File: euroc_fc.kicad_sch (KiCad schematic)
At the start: 143 parts, among them J1 Micro-Fit, J10 USB_C_Receptacle_USB2.0, J11 SWD Header, J2 Micro-Fit, J3 Micro-Fit, J4 SMA, J5 JST-GH, J6 JST-GH, J7 JST-GH, J8 JST-GH, J9 Micro_SD_Card_Det, Q1 DMN2056U, Q2 AOSP21321, Q3 DMN2056U, Q4 AOSP21321, Q5 DMN2056U, Q6 DMN2056U, Q7 DMN2056U, SW1 EVQ-PUC02K, SW2 EVQ-PUC02K, U1 STM32F401RCT6, U10 Ai-Thinker-Ra-01, U11 W25Q256JVF, U2 L7805, U3 L7805, U4 AZ1117I-3.3, U5 LSM6DSR, U6 ADXL375, U7 MS5611-01BA, U8 BMM150, U9 SAM-M8Q, Y1 25M, 18p

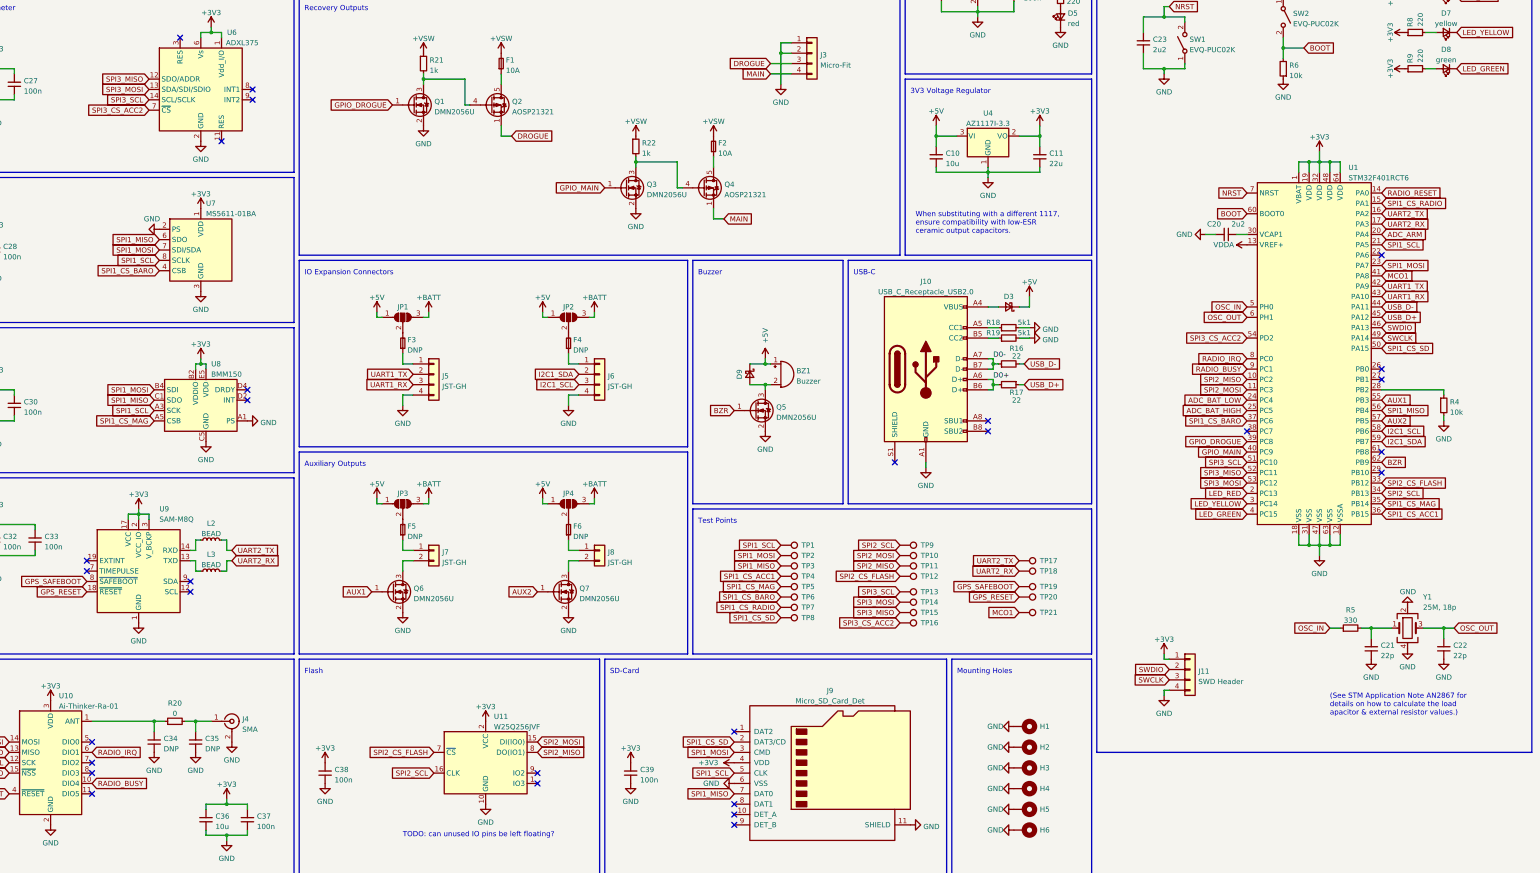
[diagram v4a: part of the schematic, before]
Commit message: Add CAN bus controller, transceiver & connectors
- Accelerometer 2 is removed from SPI for now, to be replaced
- Flash moved from SPI2 to SPI3
- SPI2 is used for CAN bus (also SD Card)
- ADC voltage dividers moved to right of PCB, IO connectors removed to
  make room
- Minor pinout changes.
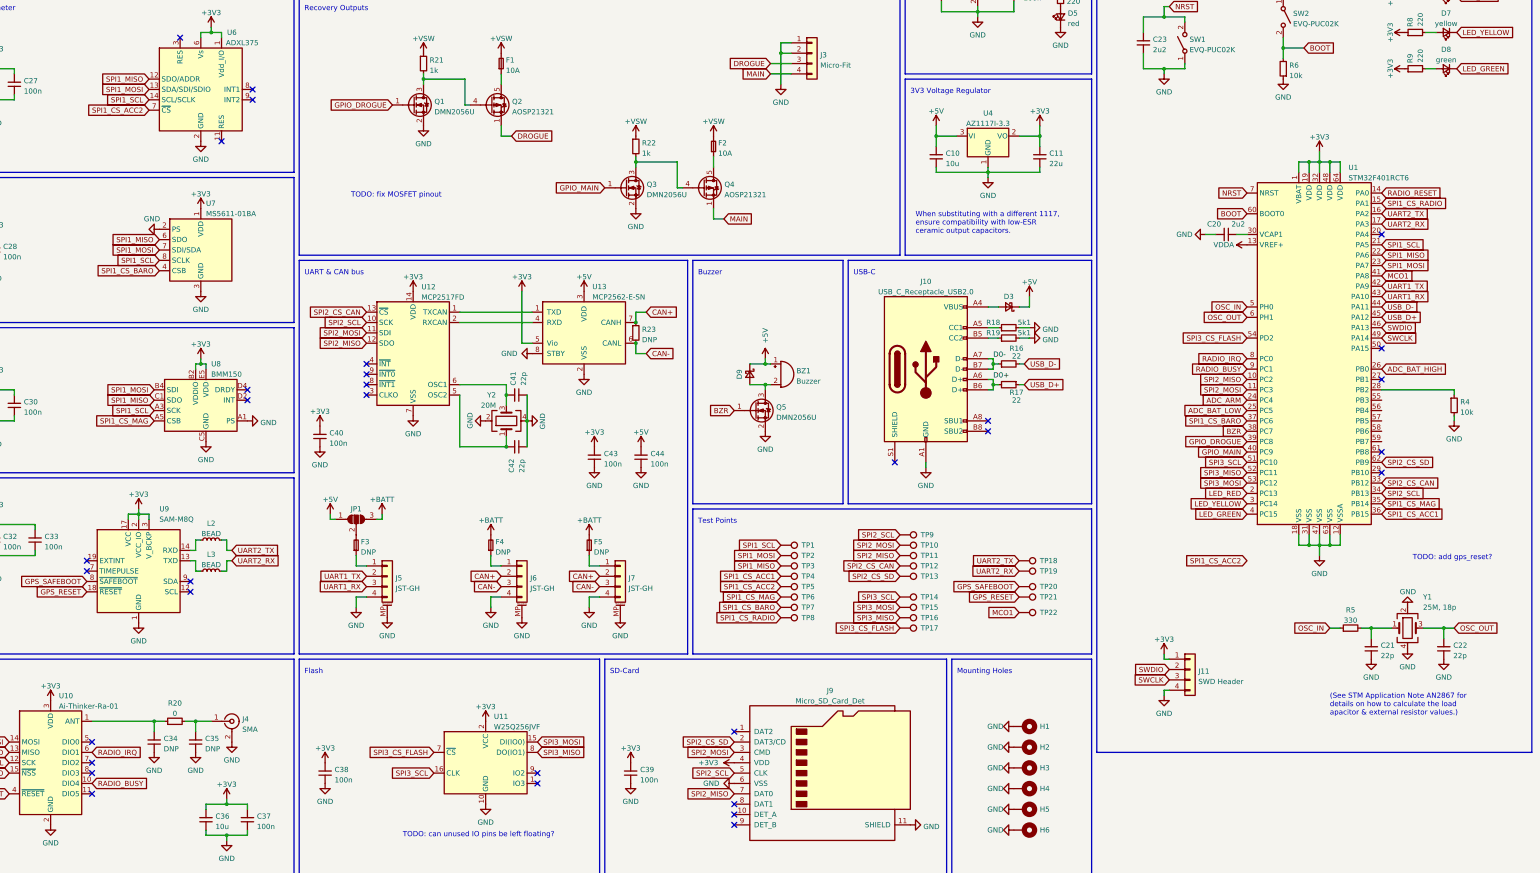
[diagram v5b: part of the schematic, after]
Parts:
- removed F6: DNP, Fuse:Fuse_1206_3216Metric, symbol Device:Fuse_Small
- removed J7, J8: JST-GH, Connector_JST:JST_GH_SM02B-GHS-TB_1x02-1MP_P1.25mm_Horizontal, symbol Connector_Generic:Conn_01x02
- removed JP2, JP3, JP4: SolderJumper_3_Open, Jumper:SolderJumper-3_P1.3mm_Open_RoundedPad1.0x1.5mm_NumberLabels, symbol Jumper:SolderJumper_3_Open
- removed Q6, Q7: DMN2056U, Package_TO_SOT_SMD:SOT-23, symbol Transistor_FET:DMG2302U
- added C40, C43, C44: 100n, Capacitor_SMD:C_0603_1608Metric, symbol Device:C_Small
- added C41, C42: 22p, Capacitor_SMD:C_0603_1608Metric, symbol Device:C_Small
- added J7: JST-GH, Connector_JST:JST_GH_SM04B-GHS-TB_1x04-1MP_P1.25mm_Horizontal, symbol Connector_Generic_MountingPin:Conn_01x04_MountingPin
- added R23: DNP, Resistor_SMD:R_0603_1608Metric, symbol Device:R_Small
- added TP22: TestPoint, TestPoint:TestPoint_Pad_D1.0mm, symbol Connector:TestPoint
- added U12: MCP2517FD, Package_SO:SOIC-14_3.9x8.7mm_P1.27mm, symbol euroc_fc:MCP2517FD
- added U13: MCP2562-E-SN, Package_SO:SOIC-8_3.9x4.9mm_P1.27mm, symbol Interface_CAN_LIN:MCP2562-E-SN
- added Y2: 20M, Oscillator:Oscillator_SMD_SeikoEpson_SG210-4Pin_2.5x2.0mm, symbol Device:Crystal_GND24
- J5, J6: symbol Connector_Generic:Conn_01x04 -> Connector_Generic_MountingPin:Conn_01x04_MountingPin
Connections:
- net +3V3: now also C40.2, C43.2, U12.14 (VDD), U13.5 (Vio)
- net +5V: now also C44.2, U13.3 (VDD)
- net +BATT: now also F4.2, F5.2
- net ADC_ARM: now also U1.24 (PC4); no longer U1.20 (PA4)
- net ADC_BAT_HIGH: now also U1.26 (PB0); no longer U1.25 (PC5)
- net ADC_BAT_LOW: now also U1.25 (PC5); no longer U1.24 (PC4)
- net BZR: now also U1.38 (PC7); no longer U1.62 (PB9)
- net GND: now also J5.MP (MountPin), J6.MP (MountPin), C40.1, C41.1, C42.1, C43.1, C44.1, J7.4 (Pin_4), J7.MP (MountPin), U12.7 (VSS), U13.2 (VSS), U13.8 (STBY), Y2.2, Y2.4
- net GPS_RESET: now also TP21.1; no longer TP20.1
- net GPS_SAFEBOOT: now also TP20.1; no longer TP19.1
- net MCO1: now also TP22.1; no longer TP21.1
- net SPI1_CS_BARO: now also TP7.1; no longer TP6.1
- net SPI1_CS_MAG: now also TP6.1; no longer TP5.1
- net SPI1_CS_RADIO: now also TP8.1; no longer TP7.1
- net SPI1_MISO: now also U1.22 (PA6), U6.12 (SDO/ADDR); no longer J9.7 (DAT0), U1.56 (PB4)
- net SPI1_MOSI: now also U6.13 (SDA/SDI/SDIO); no longer J9.3 (CMD)
- net SPI1_SCL: now also U6.14 (SCL/SCLK); no longer J9.5 (CLK)
- net SPI2_MISO: now also J9.7 (DAT0), U12.12 (SDO); no longer U11.8 (DO(IO1))
- net SPI2_MOSI: now also J9.3 (CMD), U12.11 (SDI); no longer U11.15 (DI(IO0))
- net SPI2_SCL: now also J9.5 (CLK), U12.10 (SCK); no longer U11.16 (CLK)
- net SPI3_MISO: now also TP16.1, U11.8 (DO(IO1)); no longer TP15.1, U6.12 (SDO/ADDR)
- net SPI3_MOSI: now also TP15.1, U11.15 (DI(IO0)); no longer TP14.1, U6.13 (SDA/SDI/SDIO)
- net SPI3_SCL: now also TP14.1, U11.16 (CLK); no longer TP13.1, U6.14 (SCL/SCLK)
- net UART2_RX: now also TP19.1; no longer TP18.1
- net UART2_TX: now also TP18.1; no longer TP17.1
- net at F5.1: now also J7.1 (Pin_1)
- net AUX1: no longer names the net of U1.55 (PB3)
- net AUX2: no longer names the net of U1.57 (PB5)
- net I2C1_SCL: no longer names the net of U1.58 (PB6)
- net I2C1_SCL: no longer J6.3 (Pin_3)
- net I2C1_SDA: no longer names the net of U1.59 (PB7)
- net I2C1_SDA: no longer J6.2 (Pin_2)
- removed net SPI1_CS_SD: J9.2 (DAT3/CD), TP8.1, U1.50 (PA15)
- net SPI2_CS_FLASH renamed SPI2_CS_CAN
- net SPI2_CS_CAN: now also U12.13 (~{CS}); no longer U11.7 (~{CS})
- removed net SPI3_CS_ACC2: TP16.1, U1.54 (PD2), U6.7 (~{CS})
- new net: U12.1 (TXCAN), U13.1 (TXD)
- new net: U12.2 (RXCAN), U13.4 (RXD)
- new net: C42.2, U12.5 (OSC2), Y2.1
- new net: C41.2, U12.6 (OSC1), Y2.3
- new net CAN+: J6.2 (Pin_2), J7.2 (Pin_2), R23.1, U13.7 (CANH)
- new net CAN-: J6.3 (Pin_3), J7.3 (Pin_3), R23.2, U13.6 (CANL)
- new net SPI1_CS_ACC2: TP5.1, U6.7 (~{CS})
- new net SPI2_CS_SD: J9.2 (DAT3/CD), TP13.1, U1.62 (PB9)
- new net SPI3_CS_FLASH: TP17.1, U1.54 (PD2), U11.7 (~{CS})
- no-connect marks 31 -> 34
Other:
- note added: "TODO: add gps_reset?"
- note added: "TODO: fix MOSFET pinout"
- note added: "UART & CAN bus"
- note removed: "Auxiliary Outputs"
- note removed: "IO Expansion Connectors"
- moved on the sheet: F3, F4, F5, JP1, R4, TP10, TP11, TP12, TP13, TP14, TP15, TP16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

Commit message: Replace backup acc., magnetometer
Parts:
- removed U8: BMM150, Package_CSP:WLCSP-12_1.56x1.56mm_P0.4mm, symbol Sensor_Magnetic:BMM150
- added C45: 1u, Capacitor_SMD:C_0805_2012Metric, symbol Device:C_Small
- added U8: LIS3MDL, Package_LGA:LGA-12_2x2mm_P0.5mm, symbol Sensor_Magnetic:LIS3MDL
- C20: value 2u2 -> 4u7; footprint Capacitor_SMD:C_0805_2012Metric -> Capacitor_SMD:C_1206_3216Metric; LCSC# C377773 -> C1872; Part# CL21A225KBQNNNE -> CL31B475KAHNNNE
- C23: value 2u2 -> 100n; footprint Capacitor_SMD:C_0805_2012Metric -> Capacitor_SMD:C_0603_1608Metric; LCSC# C377773 -> C1591; Part# CL21A225KBQNNNE -> CL10B104KB8NNNC
- C26: value 1u -> 10u; footprint Capacitor_SMD:C_0805_2012Metric -> Capacitor_SMD:C_1206_3216Metric; LCSC# C318694 -> C14860; Part# CL21A105KBCLNNC -> CL31B106KAHNNNE
- TP1, TP10, TP11, TP12, TP13, TP14, TP15, TP16, TP17, TP18, TP19, TP2, TP20, TP21, TP22, TP3, TP4, TP5, TP6, TP7, TP8, TP9: footprint TestPoint:TestPoint_Pad_D1.0mm -> TestPoint:TestPoint_Pad_D2.0mm
- U6: value ADXL375 -> H3LIS331DL; footprint Package_LGA:LGA-14_3x5mm_P0.8mm_LayoutBorder1x6y -> Package_LGA:LGA-16_3x3mm_P0.5mm_LayoutBorder3x5y; symbol Sensor_Motion:ADXL343 -> euroc_fc:H3LIS331DL; DigiKey# 505-ADXL375BCCZ-ND -> (none); Manufacturer Analog Devices Inc. -> (none); Part# ADXL375BCCZ -> (none)
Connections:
- net +3V3: now also U6.14 (VDD), U6.15 (reserved), C45.2, U8.5 (Vdd), U8.6 (Vdd_IO); no longer C30.2, U6.6 (Vs)
- net GND: now also U6.10 (reserved), U6.12 (GND), U6.13 (GND), U6.16 (GND), C45.1, U8.12 (GND), U8.2 (GND), U8.3 (GND); no longer U6.2 (GND), U6.4 (GND)
- net SPI1_CS_ACC2: now also U1.20 (PA4), U6.8 (~{CS}); no longer U6.7 (~{CS})
- net SPI1_CS_MAG: now also U1.29 (PB10), U8.10 (~{CS}); no longer U1.35 (PB14)
- net SPI1_MISO: now also U6.7 (SDO), U8.9 (SDO/SA1); no longer U6.12 (SDO/ADDR)
- net SPI1_MOSI: now also U6.6 (SDI), U8.11 (SDA/SDI/SDO); no longer U6.13 (SDA/SDI/SDIO)
- net SPI1_SCL: now also U6.4 (SCK), U8.1 (SCL/SPC); no longer U6.14 (SCL/SCLK)
- new net: C30.2, U8.4 (C1)
- no-connect marks 34 -> 36
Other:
- moved on the sheet: C27, C28, C29, C30, U7

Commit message: Finish rev. 2
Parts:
- C41, C42: value 22p -> 10p; LCSC# C1653 -> (none); Manufacturer Samsung Electro-Mechanics -> (none); Part# CL10C220JB8NNNC -> (none)
- Y2: footprint Oscillator:Oscillator_SMD_SeikoEpson_SG210-4Pin_2.5x2.0mm -> Crystal:Crystal_SMD_2016-4Pin_2.0x1.6mm; LCSC# C255956 -> C255878; Part# Q24FA20H0039000 -> Q22FA12800335
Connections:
- net DROGUE: now also Q2.5 (D), Q2.6 (D), Q2.7 (D), Q2.8 (D); no longer Q2.1 (S), Q2.2 (S), Q2.3 (S)
- net GPS_RESET: now also U1.61 (PB8)
- net MAIN: now also Q4.5 (D), Q4.6 (D), Q4.7 (D), Q4.8 (D); no longer Q4.1 (S), Q4.2 (S), Q4.3 (S)
- new net: F2.1, Q4.1 (S), Q4.2 (S), Q4.3 (S)
- new net: F1.1, Q2.1 (S), Q2.2 (S), Q2.3 (S)
- no-connect marks 36 -> 35
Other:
- note removed: "TODO: add gps_reset?"
- note removed: "TODO: can unused IO pins be left floating?"
- note removed: "TODO: fix MOSFET pinout"
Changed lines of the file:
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@@
   (no_connect (at 369.57 160.02))
   (no_connect (at 369.57 190.5))
-  (no_connect (at 369.57 177.8))
   (no_connect (at 369.57 170.18))
   (no_connect (at 369.57 172.72))
@@
     (effects (font (size 1.27 1.27)) (justify left bottom))
   )
-  (text "TODO: can unused IO pins be left floating?" (at 129.54 272.415 0)
-    (effects (font (size 1.27 1.27)) (justify left bottom))
-  )
   (text "USB-C" (at 240.03 134.62 0)
     (effects (font (size 1.27 1.27)) (justify left bottom))
@@
     (effects (font (size 1.27 1.27)) (justify left bottom))
   )
-  (text "TODO: add gps_reset?" (at 377.19 204.47 0)
-    (effects (font (size 1.27 1.27)) (justify left bottom))
-  )
   (text "Buzzer" (at 201.93 134.62 0)
     (effects (font (size 1.27 1.27)) (justify left bottom))
@@
     (effects (font (size 1.27 1.27)) (justify left bottom))
   )
-  (text "TODO: fix MOSFET pinout" (at 116.84 115.57 0)
-    (effects (font (size 1.27 1.27)) (justify left bottom))
-  )
   (label "D0-" (at 274.32 154.94 0)
     (effects (font (size 1.27 1.27)) (justify left bottom))
@@
     )
   )
+  (global_label "GPS_RESET" (shape input) (at 369.57 177.8 0) (fields_autoplaced)
+    (effects (font (size 1.27 1.27)) (justify left))
+    (property "Intersheet References" "${INTERSHEET_REFS}" (id 0) (at 382.4455 177.8794 0)
+      (effects (font (size 1.27 1.27)) (justify left) hide)
+    )
+  )
   (global_label "RADIO_IRQ" (shape input) (at 336.55 154.94 180) (fields_autoplaced)
     (effects (font (size 1.27 1.27)) (justify right))
@@
       (effects (font (size 1.27 1.27)) (justify right))
     )
-    (property "Value" "22p" (id 1) (at 158.75 182.88 0)
+    (property "Value" "10p" (id 1) (at 158.75 182.88 0)
       (effects (font (size 1.27 1.27)) (justify right))
     )
@@
       (effects (font (size 1.27 1.27)) hide)
     )
-    (property "LCSC#" "C1653" (id 5) (at 157.48 176.53 0)
+    (property "LCSC#" "" (id 5) (at 157.48 176.53 0)
       (effects (font (size 1.27 1.27)) hide)
     )
-    (property "Manufacturer" "Samsung Electro-Mechanics" (id 6) (at 157.48 176.53 0)
+    (property "Manufacturer" "" (id 6) (at 157.48 176.53 0)
       (effects (font (size 1.27 1.27)) hide)
     )
-    (property "Part#" "CL10C220JB8NNNC" (id 7) (at 157.48 176.53 0)
+    (property "Part#" "" (id 7) (at 157.48 176.53 0)
       (effects (font (size 1.27 1.27)) hide)
     )
@@
       (effects (font (size 1.27 1.27)) hide)
     )
-    (property "Datasheet" "https://ww1.microchip.com/downloads/en/DeviceDoc/MCP2515-Stand-Alone-CAN-Controller-with-SPI-20001801J.pdf" (id 3) (at 80.01 115.57 0)
+    (property "Datasheet" "https://www.st.com/content/ccc/resource/technical/document/datasheet/3e/48/02/c7/a4/e6/41/bb/DM00053090.pdf/files/DM00053090.pdf/jcr:content/translations/en.DM00053090.pdf" (id 3) (at 80.01 115.57 0)
       (effects (font (size 1.27 1.27)) hide)
     )
@@
   )
   (symbol (lib_id "Sensor_Magnetic:LIS3MDL") (at 76.2 161.29 0) (unit 1)
-    (in_bom yes) (on_board yes) (fields_autoplaced)
-    (property "Reference" "U8" (id 0) (at 78.2194 173.4804 0)
+    (in_bom yes) (on_board yes)
+    (property "Reference" "U8" (id 0) (at 80.01 147.32 0)
       (effects (font (size 1.27 1.27)) (justify left))
     )
-    (property "Value" "LIS3MDL" (id 1) (at 78.2194 176.0173 0)
+    (property "Value" "LIS3MDL" (id 1) (at 80.01 149.86 0)
       (effects (font (size 1.27 1.27)) (justify left))
     )
@@
       (effects (font (size 1.27 1.27)) (justify left))
     )
-    (property "Footprint" "Oscillator:Oscillator_SMD_SeikoEpson_SG210-4Pin_2.5x2.0mm" (id 2) (at 154.94 170.18 0)
+    (property "Footprint" "Crystal:Crystal_SMD_2016-4Pin_2.0x1.6mm" (id 2) (at 154.94 170.18 0)
       (effects (font (size 1.27 1.27)) hide)
     )
@@
       (effects (font (size 1.27 1.27)) hide)
     )
-    (property "Part#" "Q24FA20H0039000" (id 7) (at 154.94 170.18 0)
+    (property "Part#" "Q22FA12800335" (id 7) (at 154.94 170.18 0)
       (effects (font (size 1.27 1.27)) hide)
     )
@@
       (effects (font (size 1.27 1.27)) hide)
     )
-    (property "LCSC#" "C255956" (id 8) (at 154.94 170.18 0)
+    (property "LCSC#" "C255878" (id 8) (at 154.94 170.18 0)
       (effects (font (size 1.27 1.27)) hide)
     )
@@
     (pin "2")
   )
-  (symbol (lib_id "euroc_fc:AOSP21321") (at 151.13 92.71 0) (unit 1)
+  (symbol (lib_id "euroc_fc:AOSP21321") (at 151.13 92.71 0) (mirror x) (unit 1)
     (in_bom yes) (on_board yes) (fields_autoplaced)
     (property "Reference" "Q2" (id 0) (at 156.337 91.8753 0)
@@
       (effects (font (size 1.27 1.27)) (justify left))
     )
-    (property "Footprint" "Package_SO:SO-8_3.9x4.9mm_P1.27mm" (id 2) (at 156.21 94.615 0)
+    (property "Footprint" "Package_SO:SO-8_3.9x4.9mm_P1.27mm" (id 2) (at 156.21 90.805 0)
       (effects (font (size 1.27 1.27) italic) (justify left) hide)
     )
@@
   (symbol (lib_id "Sensor_Motion:LSM6DS3") (at 81.28 38.1 0) (unit 1)
     (in_bom yes) (on_board yes)
-    (property "Reference" "U5" (id 0) (at 86.36 22.86 0))
-    (property "Value" "LSM6DSR" (id 1) (at 88.9 25.4 0))
+    (property "Reference" "U5" (id 0) (at 86.36 20.32 0))
+    (property "Value" "LSM6DSR" (id 1) (at 88.9 22.86 0))
     (property "Footprint" "Package_LGA:LGA-14_3x2.5mm_P0.5mm_LayoutBorder3x4y" (id 2) (at 71.12 55.88 0)
       (effects (font (size 1.27 1.27)) (justify left) hide)
@@
       (effects (font (size 1.27 1.27)) (justify right))
     )
-    (property "Value" "22p" (id 1) (at 159.1758 161.5059 0)
+    (property "Value" "10p" (id 1) (at 159.1758 161.5059 0)
       (effects (font (size 1.27 1.27)) (justify right))
     )
@@
       (effects (font (size 1.27 1.27)) hide)
     )
-    (property "LCSC#" "C1653" (id 5) (at 157.48 163.83 0)
+    (property "LCSC#" "" (id 5) (at 157.48 163.83 0)
       (effects (font (size 1.27 1.27)) hide)
     )
-    (property "Manufacturer" "Samsung Electro-Mechanics" (id 6) (at 157.48 163.83 0)
+    (property "Manufacturer" "" (id 6) (at 157.48 163.83 0)
       (effects (font (size 1.27 1.27)) hide)
     )
-    (property "Part#" "CL10C220JB8NNNC" (id 7) (at 157.48 163.83 0)
+    (property "Part#" "" (id 7) (at 157.48 163.83 0)
       (effects (font (size 1.27 1.27)) hide)
     )
@@
     (pin "1")
   )
-  (symbol (lib_id "euroc_fc:AOSP21321") (at 203.2 113.03 0) (unit 1)
+  (symbol (lib_id "euroc_fc:AOSP21321") (at 203.2 113.03 0) (mirror x) (unit 1)
     (in_bom yes) (on_board yes) (fields_autoplaced)
     (property "Reference" "Q4" (id 0) (at 208.407 112.1953 0)
@@
       (effects (font (size 1.27 1.27)) (justify left))
     )
-    (property "Footprint" "Package_SO:SO-8_3.9x4.9mm_P1.27mm" (id 2) (at 208.28 114.935 0)
+    (property "Footprint" "Package_SO:SO-8_3.9x4.9mm_P1.27mm" (id 2) (at 208.28 111.125 0)
       (effects (font (size 1.27 1.27) italic) (justify left) hide)
     )
@@
     )
     (path "/d580e99a-80c1-463b-bf34-5500c566ffef"
-      (reference "C41") (unit 1) (value "22p") (footprint "Capacitor_SMD:C_0603_1608Metric")
+      (reference "C41") (unit 1) (value "10p") (footprint "Capacitor_SMD:C_0603_1608Metric")
     )
     (path "/1238c4ab-1972-4028-8c5e-61cc96a8ecfe"
-      (reference "C42") (unit 1) (value "22p") (footprint "Capacitor_SMD:C_0603_1608Metric")
+      (reference "C42") (unit 1) (value "10p") (footprint "Capacitor_SMD:C_0603_1608Metric")
     )
     (path "/87e50fc7-dacc-4aaf-af5e-46a3c37b2ac4"
@@
     )
     (path "/4289d157-0504-4815-876b-56a0606ca667"
-      (reference "Y2") (unit 1) (value "20M") (footprint "Oscillator:Oscillator_SMD_SeikoEpson_SG210-4Pin_2.5x2.0mm")
+      (reference "Y2") (unit 1) (value "20M") (footprint "Crystal:Crystal_SMD_2016-4Pin_2.0x1.6mm")
     )
   )
